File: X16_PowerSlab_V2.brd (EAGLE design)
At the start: 152.4 x 76.2 mm, 45 parts, among them J1 CONN_796636-3, J2 CONN_796636-3, J3 CONN_ET60T

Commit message: updated routing
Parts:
- moved DIODE 22.5 mm to (127.5, 30.1), turned to 270 degrees
- moved D6 21.2 mm to (123.4, 18.7), turned to 180 degrees
- moved D4 19.2 mm to (124.4, 29.3)
- moved R9 15.6 mm to (128.3, 18.7), turned to 180 degrees
- moved COUT1 15.0 mm to (130.1, 41.2), turned to 268.7 degrees
- moved C2 12.7 mm to (127.5, 35.2), turned to 270 degrees
- moved COUT3 12.5 mm to (136.2, 41.2)
- moved L1 12.4 mm to (130.1, 35.3), turned to 90 degrees
- moved R10 10.9 mm to (137.4, 12.9)
- moved D7 10.9 mm to (141.1, 12.9)
- moved CIN2 9.02 mm to (133.3, 36.2), flipped to the bottom
- moved R6 7.81 mm to (139.0, 41.2), turned to 90 degrees
- moved COUT2 7.14 mm to (133.2, 41.2), turned to 270 degrees
- moved R1 6.30 mm to (126.9, 42.4), turned to 0 degrees
- moved CIN1 5.96 mm to (136.2, 36.2), flipped to the bottom, turned to 269.2 degrees
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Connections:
- removed net 5V: U$6.7, U$6.8
- new net VIN: CIN1.+, CIN2.1, D4.C, U$2.PIN2
- net 12V: no longer CIN1.+, CIN2.1, D4.C, U$2.PIN2
- net 5.2V: now also U$6.7, U$6.8
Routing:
- net 5.2V: track 82.5 -> 0.09 mm
- net N$2: track 36.4 -> 0.00 mm, vias 1 -> 0
- net N$1: track 11.3 -> 0.00 mm
- net N$8: track 10.5 -> 0.00 mm
- net N$4: track 8.83 -> 0.00 mm
- net 12V: track 82.2 -> 78.9 mm, vias 1 -> 0
- net N$5: track 2.71 -> 0.00 mm
- net N$11: track 2.58 -> 0.06 mm
- net N$3: track 2.12 -> 0.00 mm
- net N$10: track 2.01 -> 0.00 mm
- net VIN: track 0.00 -> 0.63 mm

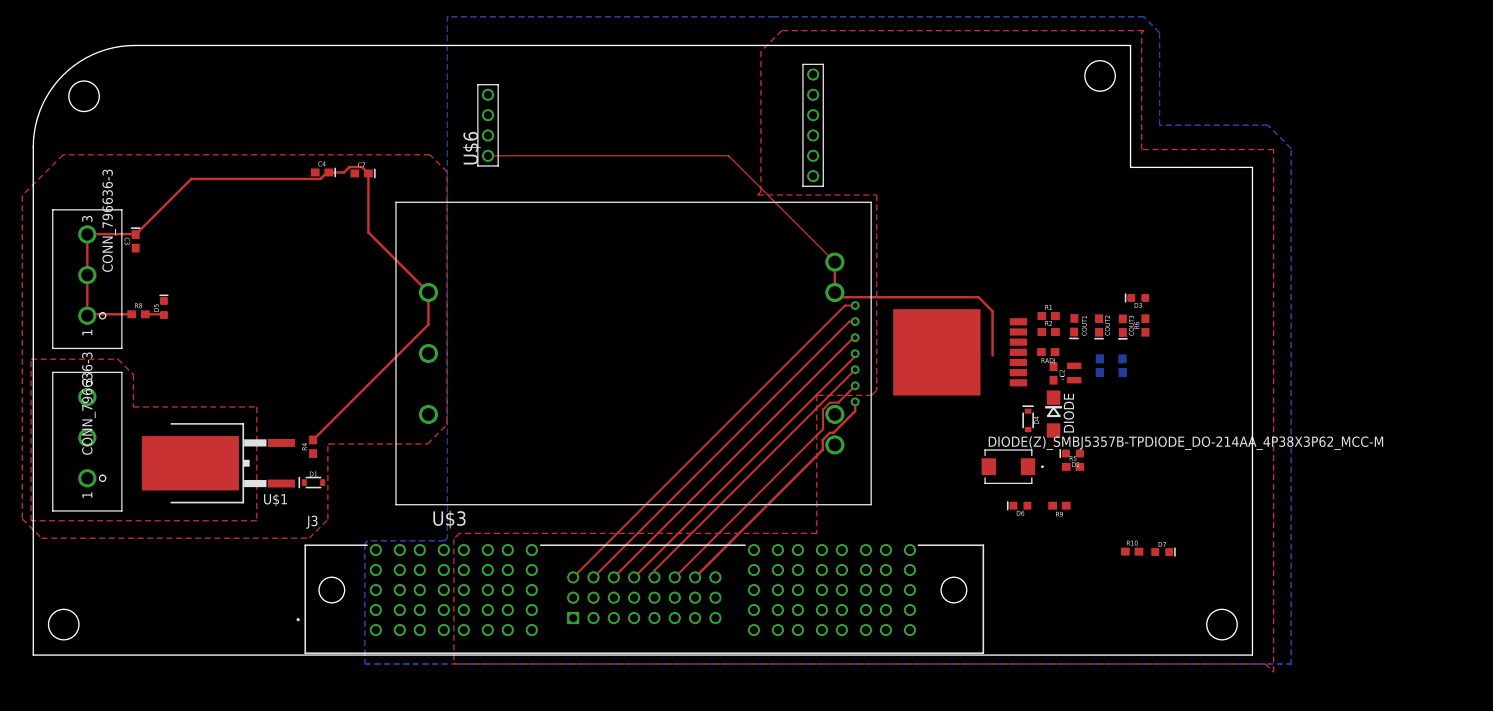
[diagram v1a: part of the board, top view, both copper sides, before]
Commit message: routing, fixed outdated components
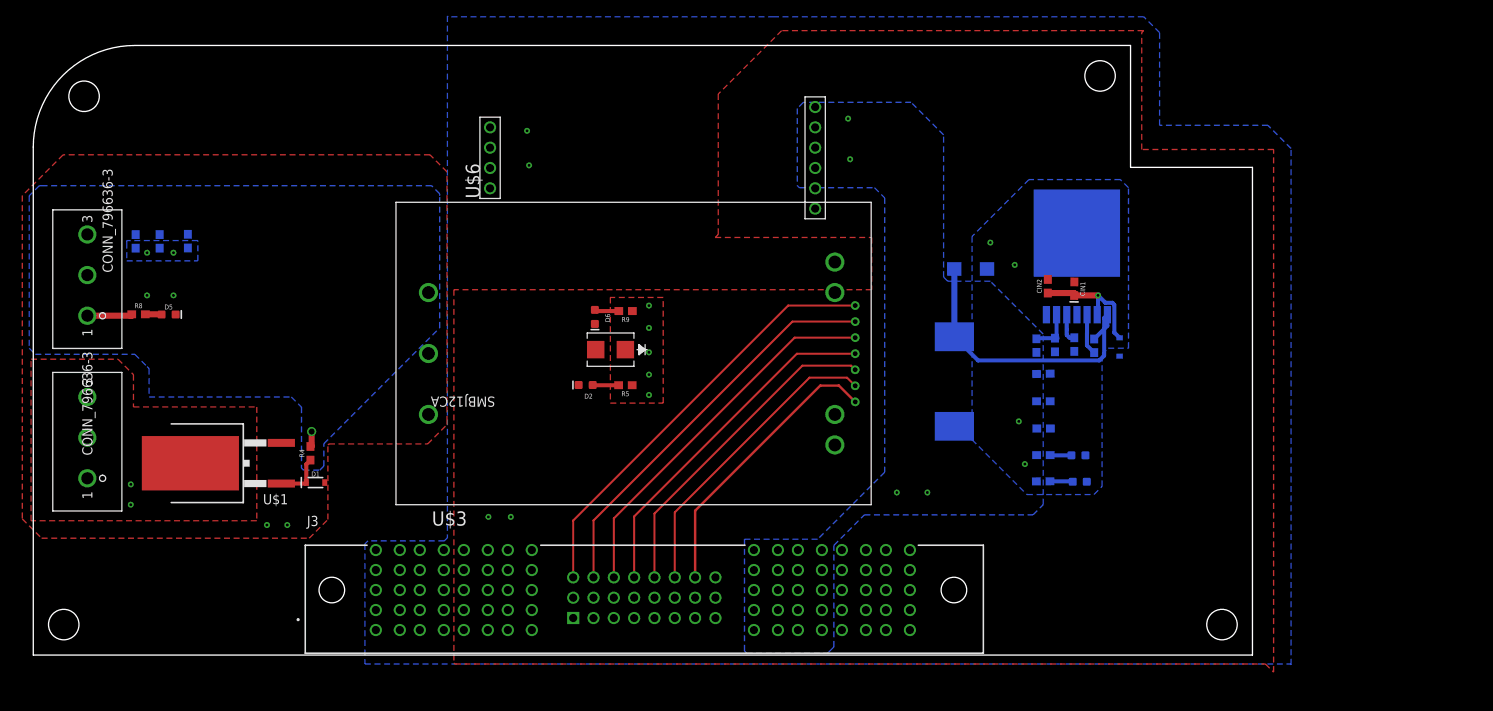
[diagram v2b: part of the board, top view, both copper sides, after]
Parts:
- CR1: value DIODE(Z)_SMBJ5357B-TPDIODE_DO-214AA_4P38X3P62_MCC-M -> SMBJ12CA; device X15_Brickstribution:DIODE_DO-214AA_4P38X3P62_MCC-M -> X16_Power_Slab:SMBJSERIES_LTF
- L1: device SparkFun-Coils:0806 -> X15-Conversion-Parts-Library:HCMA1305
- moved D2 61.5 mm to (69.0, 33.8)
- moved R9 59.4 mm to (74.0, 43.0)
- moved D6 58.2 mm to (70.2, 42.3), turned to 270 degrees
- moved R5 56.9 mm to (74.0, 33.7), turned to 180 degrees
- moved CR1 51.8 mm to (72.2, 38.2)
- moved C7 23.3 mm to (19.3, 51.7), flipped to the bottom, turned to 90 degrees
- moved C4 22.0 mm to (15.8, 51.7), flipped to the bottom, turned to 90 degrees
- moved D3 21.0 mm to (130.6, 25.0), flipped to the bottom
- moved DIODE 20.9 mm to (117.2, 48.3), flipped to the bottom, turned to 180 degrees
- moved R6 20.6 mm to (126.3, 25.0), flipped to the bottom, turned to 180 degrees
- moved COUT3 16.2 mm to (126.3, 28.3), flipped to the bottom, turned to 0 degrees
- moved L1 15.0 mm to (115.1, 34.2), flipped to the bottom, turned to 270 degrees
- moved D4 14.7 mm to (135.8, 38.5), flipped to the bottom
- moved R10 14.2 mm to (126.2, 21.7), flipped to the bottom, turned to 179.6 degrees
- moved D7 13.5 mm to (130.8, 21.7), flipped to the bottom, turned to 180 degrees
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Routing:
- net 48V: track 97.2 -> 8.02 mm, vias 0 -> 1
- net 12V: track 78.9 -> 0.00 mm, vias 0 -> 8
- net N$2: track 0.00 -> 38.4 mm
- net VIN: track 0.63 -> 16.1 mm, vias 0 -> 1
- net N$7: track 0.00 -> 6.19 mm
- net N$4: track 0.00 -> 5.48 mm
- net PMBUS_CTRL: track 30.5 -> 35.7 mm
- net N$1: track 0.00 -> 5.12 mm
- net PMBUS_SDA: track 36.3 -> 40.9 mm
- net PMBUS_SCL: track 42.6 -> 46.9 mm
- net PMBUS_SALERT: track 39.4 -> 43.7 mm
- net PMBUS_GND: track 33.9 -> 38.1 mm
- net PMBUS_SA1: track 46.0 -> 50.1 mm
- net PMBUS_SA0: track 49.3 -> 53.5 mm
- net N$8: track 0.00 -> 3.62 mm
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- added copper zone on layer 1, net 12V
- added copper zone on layer 16, net 48V
- added copper zone on layer 16, net 48V_GND
- added copper zone on layer 16, net 5.2V
- added copper zone on layer 16, net GND

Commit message: updated board
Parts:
- removed COUT1, COUT2, COUT3: 150uF, SparkFun-Capacitors:0603-POLAR
- added COUT4, COUT5, COUT6: 150uF, X15-Conversion-Parts-Library:2917(7343-31-METRIC)
- CIN1: value 180uF -> 150uF; device SparkFun-Capacitors:0603-POLAR -> X15-Conversion-Parts-Library:2917(7343-31-METRIC)
- moved L1 27.2 mm to (142.3, 32.9)
- moved DIODE 21.4 mm to (138.3, 44.7), turned to 90 degrees
- moved R10 13.6 mm to (128.9, 8.38), turned to 89.6 degrees
- moved D3 11.5 mm to (129.9, 13.5)
- moved R6 11.4 mm to (126.5, 13.6)
- moved D7 10.5 mm to (129.8, 11.3)
- moved CIN1 10.0 mm to (120.7, 49.0), turned to 90 degrees
- moved D4 9.56 mm to (129.7, 45.9), flipped to the top, turned to 90 degrees
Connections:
- net 5.2V: now also COUT4.+, COUT5.+, COUT6.+; no longer COUT1.+, COUT2.+, COUT3.+
- net GND: now also COUT4.-, COUT5.-, COUT6.-; no longer COUT1.-, COUT2.-, COUT3.-
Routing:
- net N$2: track 38.4 -> 3.72 mm
- net VIN: track 16.1 -> 0.14 mm, vias 1 -> 0
- net N$5: track 2.68 -> 1.66 mm
- net N$11: track 2.97 -> 2.09 mm
- removed copper zone on layer 16, net GND

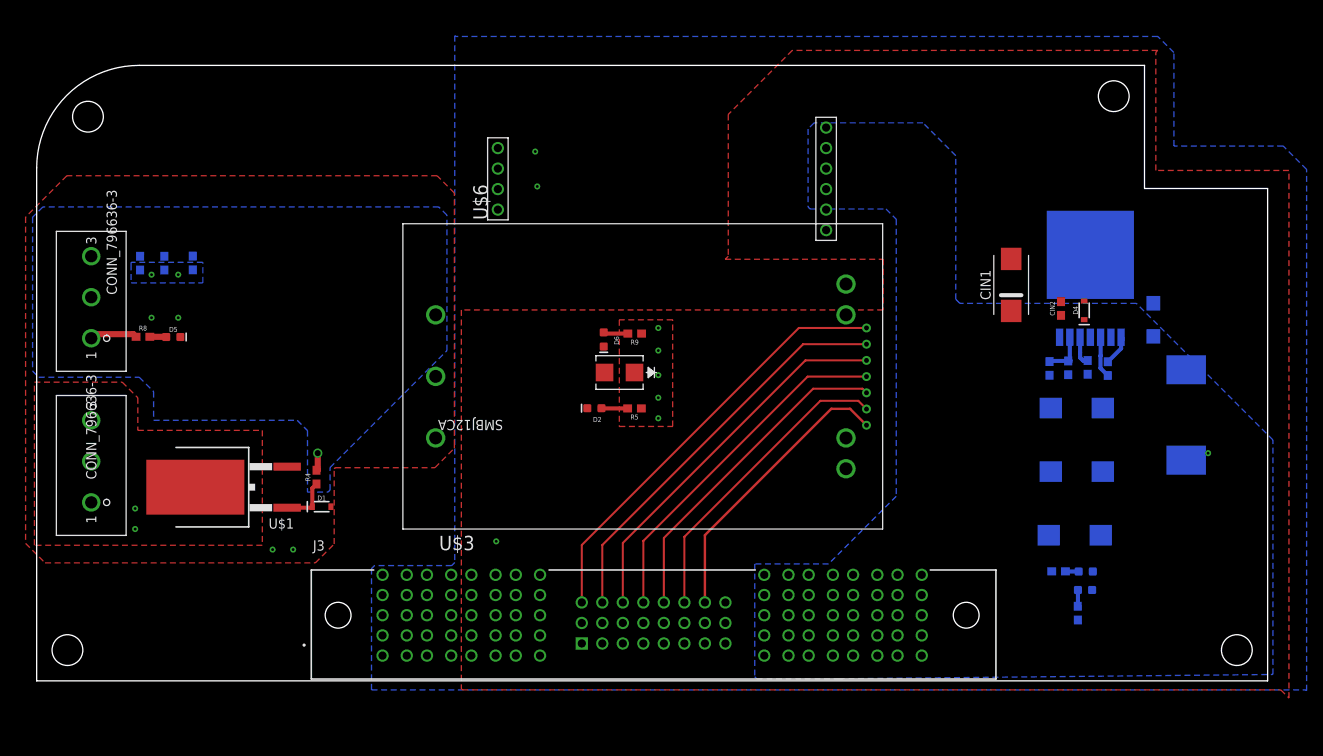
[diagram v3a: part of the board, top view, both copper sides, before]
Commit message: finished polygons
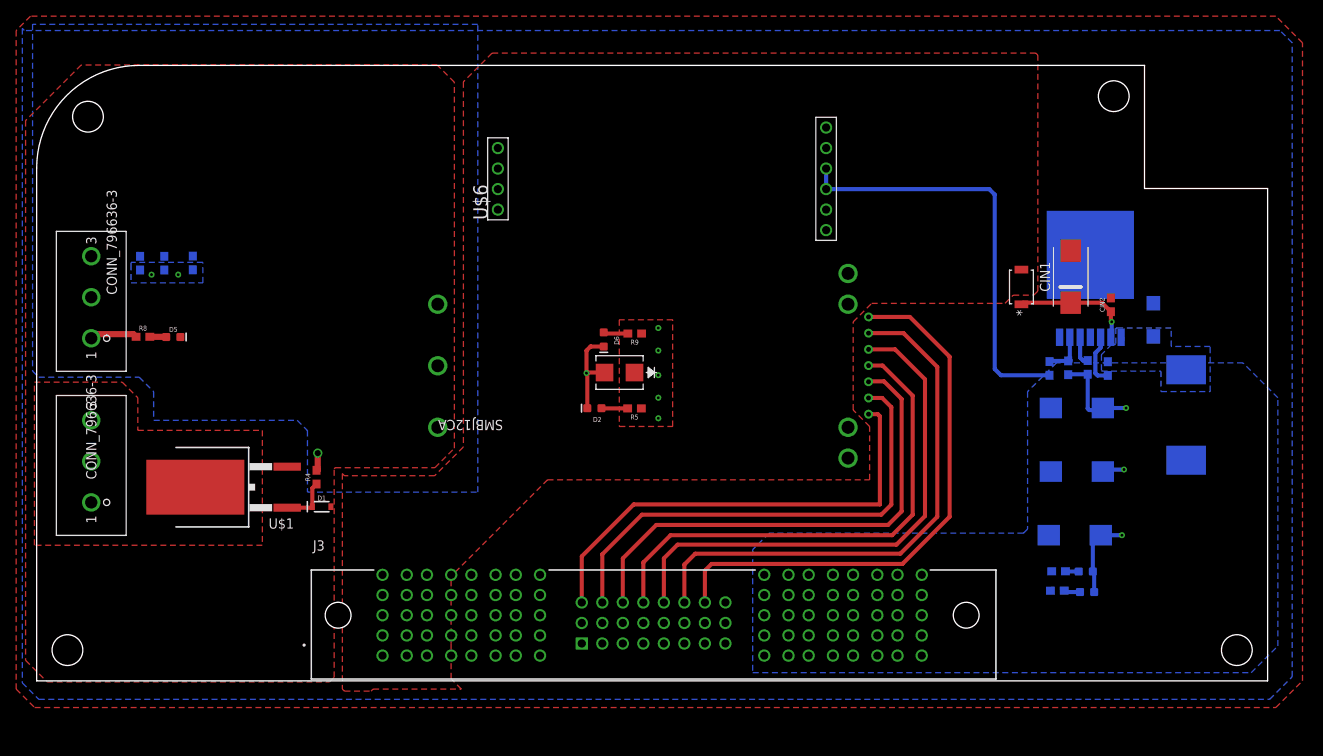
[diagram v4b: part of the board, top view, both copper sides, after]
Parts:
- removed D4: 250mA/100V, SparkFun-DiscreteSemi:SOD-323
- added CR2: RBS2MM40CTR, X16_Power_Slab:SDO_RBS2MM40CTR_ROM
- moved U$3 39.1 mm to (45.6, 57.9), flipped to the bottom, turned to 180 degrees
- moved CIN1 7.44 mm to (128.0, 50.0)
- moved CIN2 6.19 mm to (133.0, 46.6)
- moved R10 3.78 mm to (126.4, 11.2), turned to 179.6 degrees
- moved D7 0.36 mm to (130.0, 11.0)
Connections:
- net 12V: now also CR2.2; no longer D4.A
- net 48V_GND: now also U$3.PIN2
- net VIN: now also CR2.1; no longer D4.C
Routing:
- net 5.2V: track 0.00 -> 52.4 mm, vias 1 -> 0
- net GND: track 0.00 -> 36.2 mm, vias 0 -> 4
- net PMBUS_CTRL: track 35.7 -> 68.9 mm
- net PMBUS_GND: track 38.1 -> 67.3 mm
- net PMBUS_SDA: track 40.9 -> 65.4 mm
- net PMBUS_SALERT: track 43.7 -> 62.5 mm
- net VIN: track 0.14 -> 14.9 mm, vias 0 -> 1
- net PMBUS_SCL: track 46.9 -> 61.3 mm
- net PMBUS_SA1: track 50.1 -> 59.7 mm
- net PMBUS_SA0: track 53.5 -> 57.7 mm
- net N$2: track 3.72 -> 0.38 mm
- net N$1: track 5.12 -> 6.39 mm
- added copper zone on layer 16, net GND
- added copper zone on layer 16, net N$2
- removed copper zone on layer 16, net 12V

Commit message: deleted v1
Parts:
- moved 48VGND_TP 71.8 mm to (-70.6, -26.9)
- moved 12VGND_TP 71.8 mm to (-69.9, -31.0)
- moved 12V_TP 71.8 mm to (-68.6, -27.3)
- moved 48_TP 71.8 mm to (-72.1, -29.3)
- moved TP5 71.8 mm to (-68.6, -30.4)
- moved TP6 71.8 mm to (-71.3, -30.3)
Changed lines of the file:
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@@
 <attribute name="NAME" x="55.8292" y="57.0738" size="1.778" layer="25" rot="R90"/>
 </element>
-<element name="48_TP" library="SparkFun-Connectors" library_urn="urn:adsk.eagle:library:513" package="PAD.03X.05" package3d_urn="urn:adsk.eagle:package:38285/2" value="TEST-POINT3X5" x="-1.524" y="-16.3576" smashed="yes"/>
-<element name="48VGND_TP" library="SparkFun-Connectors" library_urn="urn:adsk.eagle:library:513" package="PAD.03X.05" package3d_urn="urn:adsk.eagle:package:38285/2" value="TEST-POINT3X5" x="0.0254" y="-13.9192" smashed="yes"/>
-<element name="12V_TP" library="SparkFun-Connectors" library_urn="urn:adsk.eagle:library:513" package="PAD.03X.05" package3d_urn="urn:adsk.eagle:package:38285/2" value="TEST-POINT3X5" x="2.0574" y="-14.351" smashed="yes"/>
-<element name="12VGND_TP" library="SparkFun-Connectors" library_urn="urn:adsk.eagle:library:513" package="PAD.03X.05" package3d_urn="urn:adsk.eagle:package:38285/2" value="TEST-POINT3X5" x="0.6858" y="-18.0086" smashed="yes"/>
-<element name="TP5" library="SparkFun-Connectors" library_urn="urn:adsk.eagle:library:513" package="PAD.03X.05" package3d_urn="urn:adsk.eagle:package:38285/2" value="TEST-POINT3X5" x="1.9812" y="-17.399" smashed="yes"/>
-<element name="TP6" library="SparkFun-Connectors" library_urn="urn:adsk.eagle:library:513" package="PAD.03X.05" package3d_urn="urn:adsk.eagle:package:38285/2" value="TEST-POINT3X5" x="-0.6858" y="-17.3736" smashed="yes"/>
+<element name="48_TP" library="SparkFun-Connectors" library_urn="urn:adsk.eagle:library:513" package="PAD.03X.05" package3d_urn="urn:adsk.eagle:package:38285/2" value="TEST-POINT3X5" x="-72.136" y="-29.3116" smashed="yes"/>
+<element name="48VGND_TP" library="SparkFun-Connectors" library_urn="urn:adsk.eagle:library:513" package="PAD.03X.05" package3d_urn="urn:adsk.eagle:package:38285/2" value="TEST-POINT3X5" x="-70.5866" y="-26.8732" smashed="yes"/>
+<element name="12V_TP" library="SparkFun-Connectors" library_urn="urn:adsk.eagle:library:513" package="PAD.03X.05" package3d_urn="urn:adsk.eagle:package:38285/2" value="TEST-POINT3X5" x="-68.5546" y="-27.305" smashed="yes"/>
+<element name="12VGND_TP" library="SparkFun-Connectors" library_urn="urn:adsk.eagle:library:513" package="PAD.03X.05" package3d_urn="urn:adsk.eagle:package:38285/2" value="TEST-POINT3X5" x="-69.9262" y="-30.9626" smashed="yes"/>
+<element name="TP5" library="SparkFun-Connectors" library_urn="urn:adsk.eagle:library:513" package="PAD.03X.05" package3d_urn="urn:adsk.eagle:package:38285/2" value="TEST-POINT3X5" x="-68.6308" y="-30.353" smashed="yes"/>
+<element name="TP6" library="SparkFun-Connectors" library_urn="urn:adsk.eagle:library:513" package="PAD.03X.05" package3d_urn="urn:adsk.eagle:package:38285/2" value="TEST-POINT3X5" x="-71.2978" y="-30.3276" smashed="yes"/>
 <element name="L1" library="X15-Conversion-Parts-Library" package="HCMA1305" package3d_urn="urn:adsk.eagle:package:24201702/2" value="15uH" x="142.3162" y="32.9184" smashed="yes" rot="MR270">
 <attribute name="NAME" x="125.6792" y="28.2702" size="1.27" layer="26" rot="MR270" align="bottom-center"/>
@@
 <contactref element="C7" pad="-"/>
 <polygon width="0.1524" layer="1" isolate="0.3048" rank="2">
-<vertex x="-1.3716" y="69.3674"/>
-<vertex x="-1.3716" y="2.54"/>
+<vertex x="1.2954" y="72.0344"/>
 <vertex x="1.2954" y="-0.127"/>
 <vertex x="36.2712" y="-0.127"/>
